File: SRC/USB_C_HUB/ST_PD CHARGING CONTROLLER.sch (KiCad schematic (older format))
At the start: 16 parts, among them Q9 STL6P3LLH6, U12 STUSB4500QTR

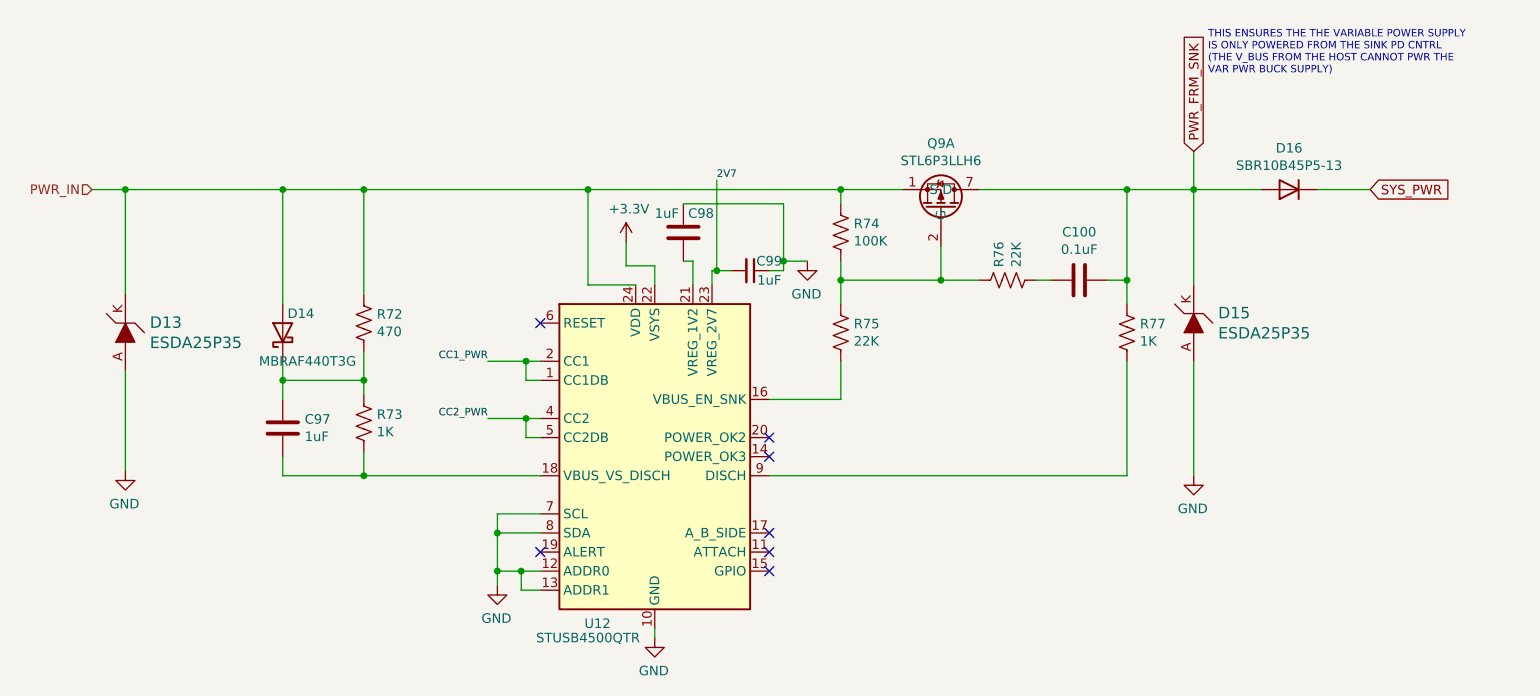
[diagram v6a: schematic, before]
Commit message: schematic capture complete. Pending Footprint assignment. accetable Errors=21
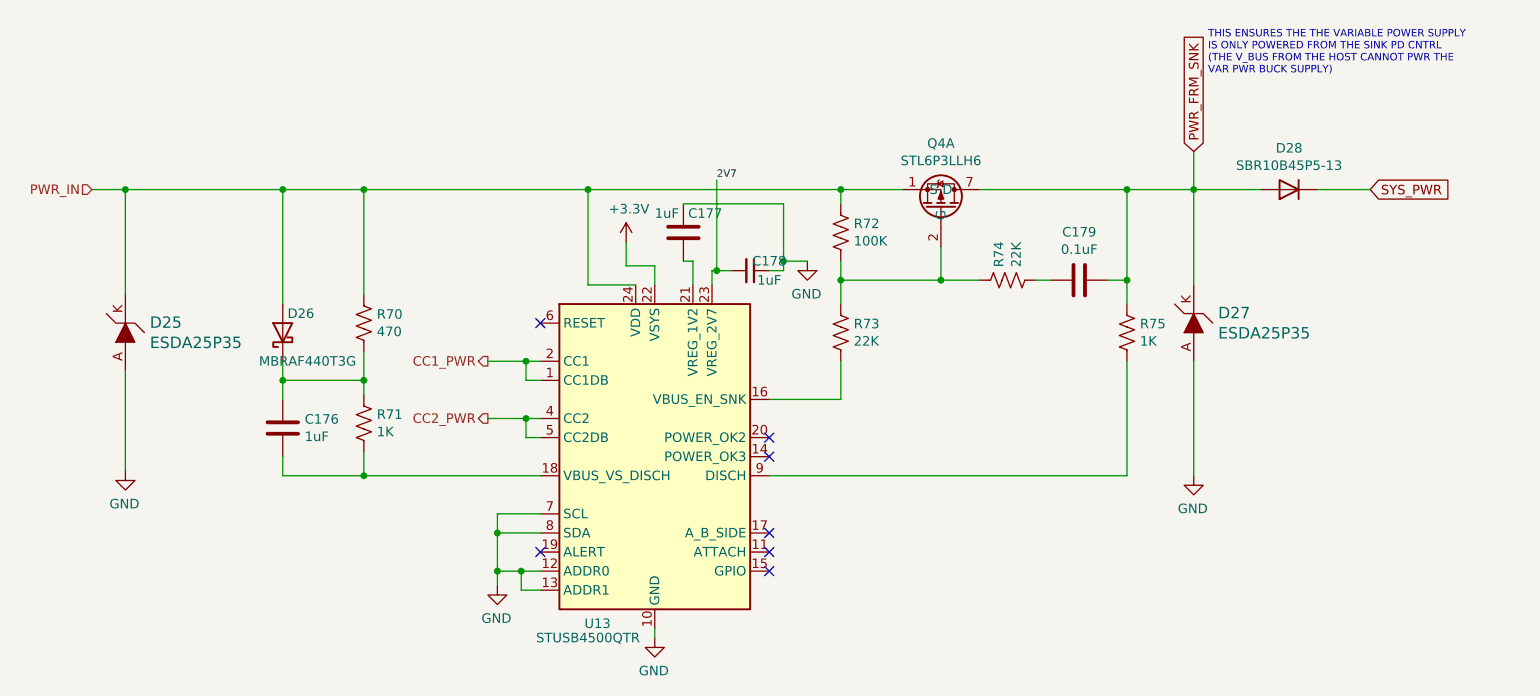
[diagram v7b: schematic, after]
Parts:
- renumbered C97 to C176, C98 to C177, C99 to C178, C100 to C179, D13 to D25, D14 to D26, D15 to D27, D16 to D28, Q9 to Q4, R72 to R70, R73 to R71, R74 to R72, R75 to R73, R76 to R74, R77 to R75, U12 to U13
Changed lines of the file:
@@
 $Descr A4 11693 8268
 encoding utf-8
-Sheet 8 15
+Sheet 13 15
 Title ""
 Date ""
@@
 P 2800 2275
 AR Path="/61DE3B32" Ref="R?"  Part="1"
-AR Path="/61DDBD9F/61DE3B32" Ref="R72"  Part="1"
-F 0 "R72" H 2868 2321 50  0000 L CNN
+AR Path="/61DDBD9F/61DE3B32" Ref="R70"  Part="1"
+F 0 "R70" H 2868 2321 50  0000 L CNN
 F 1 "470" H 2868 2230 50  0000 L CNN
 F 2 "" V 2840 2265 50  0001 C CNN
@@
 P 2375 2825
 AR Path="/61DE3B39" Ref="C?"  Part="1"
-AR Path="/61DDBD9F/61DE3B39" Ref="C97"  Part="1"
-F 0 "C97" H 2490 2871 50  0000 L CNN
+AR Path="/61DDBD9F/61DE3B39" Ref="C176"  Part="1"
+F 0 "C176" H 2490 2871 50  0000 L CNN
 F 1 "1uF" H 2490 2780 50  0000 L CNN
 F 2 "" H 2413 2675 50  0001 C CNN
@@
 P 2800 2800
 AR Path="/61DE3B3F" Ref="R?"  Part="1"
-AR Path="/61DDBD9F/61DE3B3F" Ref="R73"  Part="1"
-F 0 "R73" H 2868 2846 50  0000 L CNN
+AR Path="/61DDBD9F/61DE3B3F" Ref="R71"  Part="1"
+F 0 "R71" H 2868 2846 50  0000 L CNN
 F 1 "1K" H 2868 2755 50  0000 L CNN
 F 2 "" V 2840 2790 50  0001 C CNN
@@
 P 2375 2325
 AR Path="/61DE3B46" Ref="D?"  Part="1"
-AR Path="/61DDBD9F/61DE3B46" Ref="D14"  Part="1"
-F 0 "D14" V 2475 2300 50  0000 R CNN
+AR Path="/61DDBD9F/61DE3B46" Ref="D26"  Part="1"
+F 0 "D26" V 2475 2300 50  0000 R CNN
 F 1 "MBRAF440T3G" V 2225 2450 50  0000 R CNN
 F 2 "" H 2375 2325 50  0001 C CNN
@@
 P 4175 1850
 AR Path="/61DE3B5D" Ref="#PWR?"  Part="1"
-AR Path="/61DDBD9F/61DE3B5D" Ref="#PWR0194"  Part="1"
-F 0 "#PWR0194" H 4175 1700 50  0001 C CNN
+AR Path="/61DDBD9F/61DE3B5D" Ref="#PWR0167"  Part="1"
+F 0 "#PWR0167" H 4175 1700 50  0001 C CNN
 F 1 "+3.3V" H 4190 2023 50  0000 C CNN
 F 2 "" H 4175 1850 60  0000 C CNN
@@
 P 6075 1575
 AR Path="/61DE3B63" Ref="Q?"  Part="1"
-AR Path="/61DDBD9F/61DE3B63" Ref="Q9"  Part="1"
-F 0 "Q9" V 6317 1325 50  0000 C CNN
+AR Path="/61DDBD9F/61DE3B63" Ref="Q4"  Part="1"
+F 0 "Q4" V 6317 1325 50  0000 C CNN
 F 1 "STL6P3LLH6" V 6226 1325 50  0000 C CNN
 F 2 "" H 6075 1575 50  0001 C CNN
@@
 P 5300 1800
 AR Path="/61DE3B69" Ref="R?"  Part="1"
-AR Path="/61DDBD9F/61DE3B69" Ref="R74"  Part="1"
-F 0 "R74" H 5368 1846 50  0000 L CNN
+AR Path="/61DDBD9F/61DE3B69" Ref="R72"  Part="1"
+F 0 "R72" H 5368 1846 50  0000 L CNN
 F 1 "100K" H 5368 1755 50  0000 L CNN
 F 2 "" V 5340 1790 50  0001 C CNN
@@
 P 5300 2325
 AR Path="/61DE3B6F" Ref="R?"  Part="1"
-AR Path="/61DDBD9F/61DE3B6F" Ref="R75"  Part="1"
-F 0 "R75" H 5368 2371 50  0000 L CNN
+AR Path="/61DDBD9F/61DE3B6F" Ref="R73"  Part="1"
+F 0 "R73" H 5368 2371 50  0000 L CNN
 F 1 "22K" H 5368 2280 50  0000 L CNN
 F 2 "" V 5340 2315 50  0001 C CNN
@@
 P 6175 2050
 AR Path="/61DE3B7B" Ref="R?"  Part="1"
-AR Path="/61DDBD9F/61DE3B7B" Ref="R76"  Part="1"
-F 0 "R76" H 6243 2096 50  0000 L CNN
+AR Path="/61DDBD9F/61DE3B7B" Ref="R74"  Part="1"
+F 0 "R74" H 6243 2096 50  0000 L CNN
 F 1 "22K" H 6243 2005 50  0000 L CNN
 F 2 "" V 6215 2040 50  0001 C CNN
@@
 P 6550 2050
 AR Path="/61DE3B87" Ref="C?"  Part="1"
-AR Path="/61DDBD9F/61DE3B87" Ref="C100"  Part="1"
-F 0 "C100" V 6802 2050 50  0000 C CNN
+AR Path="/61DDBD9F/61DE3B87" Ref="C179"  Part="1"
+F 0 "C179" V 6802 2050 50  0000 C CNN
 F 1 "0.1uF" V 6711 2050 50  0000 C CNN
 F 2 "" H 6588 1900 50  0001 C CNN
@@
 AR Path="/619540C6/61DE3B8E" Ref="#PWR?"  Part="1"
 AR Path="/61DE3B8E" Ref="#PWR?"  Part="1"
-AR Path="/61DDBD9F/61DE3B8E" Ref="#PWR0195"  Part="1"
-F 0 "#PWR0195" H 4325 3675 50  0001 C CNN
+AR Path="/61DDBD9F/61DE3B8E" Ref="#PWR0168"  Part="1"
+F 0 "#PWR0168" H 4325 3675 50  0001 C CNN
 F 1 "GND" H 4330 3752 50  0000 C CNN
 F 2 "" H 4325 3925 60  0000 C CNN
@@
 AR Path="/619540C6/61DE3B95" Ref="#PWR?"  Part="1"
 AR Path="/61DE3B95" Ref="#PWR?"  Part="1"
-AR Path="/61DDBD9F/61DE3B95" Ref="#PWR0196"  Part="1"
-F 0 "#PWR0196" H 5125 1700 50  0001 C CNN
+AR Path="/61DDBD9F/61DE3B95" Ref="#PWR0169"  Part="1"
+F 0 "#PWR0169" H 5125 1700 50  0001 C CNN
 F 1 "GND" H 5130 1777 50  0000 C CNN
 F 2 "" H 5125 1950 60  0000 C CNN
@@
 P 4825 2000
 AR Path="/61DE3B9B" Ref="C?"  Part="1"
-AR Path="/61DDBD9F/61DE3B9B" Ref="C99"  Part="1"
-F 0 "C99" V 4775 2100 50  0000 C CNN
+AR Path="/61DDBD9F/61DE3B9B" Ref="C178"  Part="1"
+F 0 "C178" V 4775 2100 50  0000 C CNN
 F 1 "1uF" V 4875 2100 50  0000 C CNN
 F 2 "" H 4825 2000 50  0001 C CNN
@@
 P 6800 2325
 AR Path="/61DE3BA7" Ref="R?"  Part="1"
-AR Path="/61DDBD9F/61DE3BA7" Ref="R77"  Part="1"
-F 0 "R77" H 6868 2371 50  0000 L CNN
+AR Path="/61DDBD9F/61DE3BA7" Ref="R75"  Part="1"
+F 0 "R75" H 6868 2371 50  0000 L CNN
 F 1 "1K" H 6868 2280 50  0000 L CNN
 F 2 "" V 6840 2315 50  0001 C CNN
@@
 AR Path="/61C45066/61DE3BBC" Ref="D?"  Part="1"
 AR Path="/61DE3BBC" Ref="D?"  Part="1"
-AR Path="/61DDBD9F/61DE3BBC" Ref="D15"  Part="1"
-F 0 "D15" V 7203 2147 60  0000 R CNN
+AR Path="/61DDBD9F/61DE3BBC" Ref="D27"  Part="1"
+F 0 "D27" V 7203 2147 60  0000 R CNN
 F 1 "ESDA25P35" V 7097 2147 60  0000 R CNN
 F 2 "digikey-footprints:SOD-523" H 7350 2475 60  0001 L CNN
@@
 Wire Wire Line
 	4925 3075 6800 3075
-Text Label 3450 2475 2    39   ~ 0
-CC1_PWR
-Text Label 3450 2775 2    39   ~ 0
-CC2_PWR
 Wire Wire Line
 	3725 2475 3650 2475
@@
 AR Path="/619540C6/61DE3BD5" Ref="#PWR?"  Part="1"
 AR Path="/61DE3BD5" Ref="#PWR?"  Part="1"
-AR Path="/61DDBD9F/61DE3BD5" Ref="#PWR0197"  Part="1"
-F 0 "#PWR0197" H 3500 3400 50  0001 C CNN
+AR Path="/61DDBD9F/61DE3BD5" Ref="#PWR0166"  Part="1"
+F 0 "#PWR0166" H 3500 3400 50  0001 C CNN
 F 1 "GND" H 3505 3477 50  0000 C CNN
 F 2 "" H 3500 3650 60  0000 C CNN
@@
 P 4475 1800
 AR Path="/61DE3BE2" Ref="C?"  Part="1"
-AR Path="/61DDBD9F/61DE3BE2" Ref="C98"  Part="1"
-F 0 "C98" H 4500 1900 50  0000 L CNN
+AR Path="/61DDBD9F/61DE3BE2" Ref="C177"  Part="1"
+F 0 "C177" H 4500 1900 50  0000 L CNN
 F 1 "1uF" H 4325 1900 50  0000 L CNN
 F 2 "" H 4513 1650 50  0001 C CNN
@@
 P 4325 2975
 AR Path="/61DE3BF7" Ref="U?"  Part="1"
-AR Path="/61DDBD9F/61DE3BF7" Ref="U12"  Part="1"
-F 0 "U12" H 4025 2100 50  0000 C CNN
+AR Path="/61DDBD9F/61DE3BF7" Ref="U13"  Part="1"
+F 0 "U13" H 4025 2100 50  0000 C CNN
 F 1 "STUSB4500QTR" H 3975 2025 50  0000 C CNN
 F 2 "Package_DFN_QFN:QFN-24-1EP_4x4mm_P0.5mm_EP2.7x2.7mm" H 4325 2975 50  0001 C CNN
@@
 Connection ~ 7150 1575
 $Comp
-L Device:D D16
+L Device:D D28
 U 1 1 61E1CE99
 P 7650 1575
-F 0 "D16" H 7650 1358 50  0000 C CNN
+F 0 "D28" H 7650 1358 50  0000 C CNN
 F 1 "SBR10B45P5-13" H 7650 1449 50  0000 C CNN
 F 2 "" H 7650 1575 50  0001 C CNN
@@
 AR Path="/61C45066/61F50F14" Ref="D?"  Part="1"
 AR Path="/61F50F14" Ref="D?"  Part="1"
-AR Path="/61DDBD9F/61F50F14" Ref="D13"  Part="1"
-F 0 "D13" V 1603 2197 60  0000 R CNN
+AR Path="/61DDBD9F/61F50F14" Ref="D25"  Part="1"
+F 0 "D25" V 1603 2197 60  0000 R CNN
 F 1 "ESDA25P35" V 1497 2197 60  0000 R CNN
 F 2 "digikey-footprints:SOD-523" H 1750 2525 60  0001 L CNN
@@
 AR Path="/619540C6/61F58B30" Ref="#PWR?"  Part="1"
 AR Path="/61F58B30" Ref="#PWR?"  Part="1"
-AR Path="/61DDBD9F/61F58B30" Ref="#PWR0198"  Part="1"
-F 0 "#PWR0198" H 7150 2825 50  0001 C CNN
+AR Path="/61DDBD9F/61F58B30" Ref="#PWR0170"  Part="1"
+F 0 "#PWR0170" H 7150 2825 50  0001 C CNN
 F 1 "GND" H 7155 2902 50  0000 C CNN
 F 2 "" H 7150 3075 60  0000 C CNN
@@
 AR Path="/619540C6/61F5A776" Ref="#PWR?"  Part="1"
 AR Path="/61F5A776" Ref="#PWR?"  Part="1"
-AR Path="/61DDBD9F/61F5A776" Ref="#PWR0199"  Part="1"
-F 0 "#PWR0199" H 1550 2800 50  0001 C CNN
+AR Path="/61DDBD9F/61F5A776" Ref="#PWR0165"  Part="1"
+F 0 "#PWR0165" H 1550 2800 50  0001 C CNN
 F 1 "GND" H 1555 2877 50  0000 C CNN
 F 2 "" H 1550 3050 60  0000 C CNN
@@
 Text Notes 7225 975  0    39   ~ 0
 THIS ENSURES THE THE VARIABLE POWER SUPPLY\nIS ONLY POWERED FROM THE SINK PD CNTRL\n(THE V_BUS FROM THE HOST CANNOT PWR THE\nVAR PWR BUCK SUPPLY)
+Text HLabel 3450 2475 0    50   Output ~ 0
+CC1_PWR
+Text HLabel 3450 2775 0    50   Output ~ 0
+CC2_PWR
 $EndSCHEMATC
